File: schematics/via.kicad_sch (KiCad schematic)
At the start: 8 parts, among them SW1 SW_DIP_x08, SW2 SW_Push, SW3 SW_Push, SW5 SW_Push, SW6 SW_Push, U27 W65C22SxP, U28 74HC14

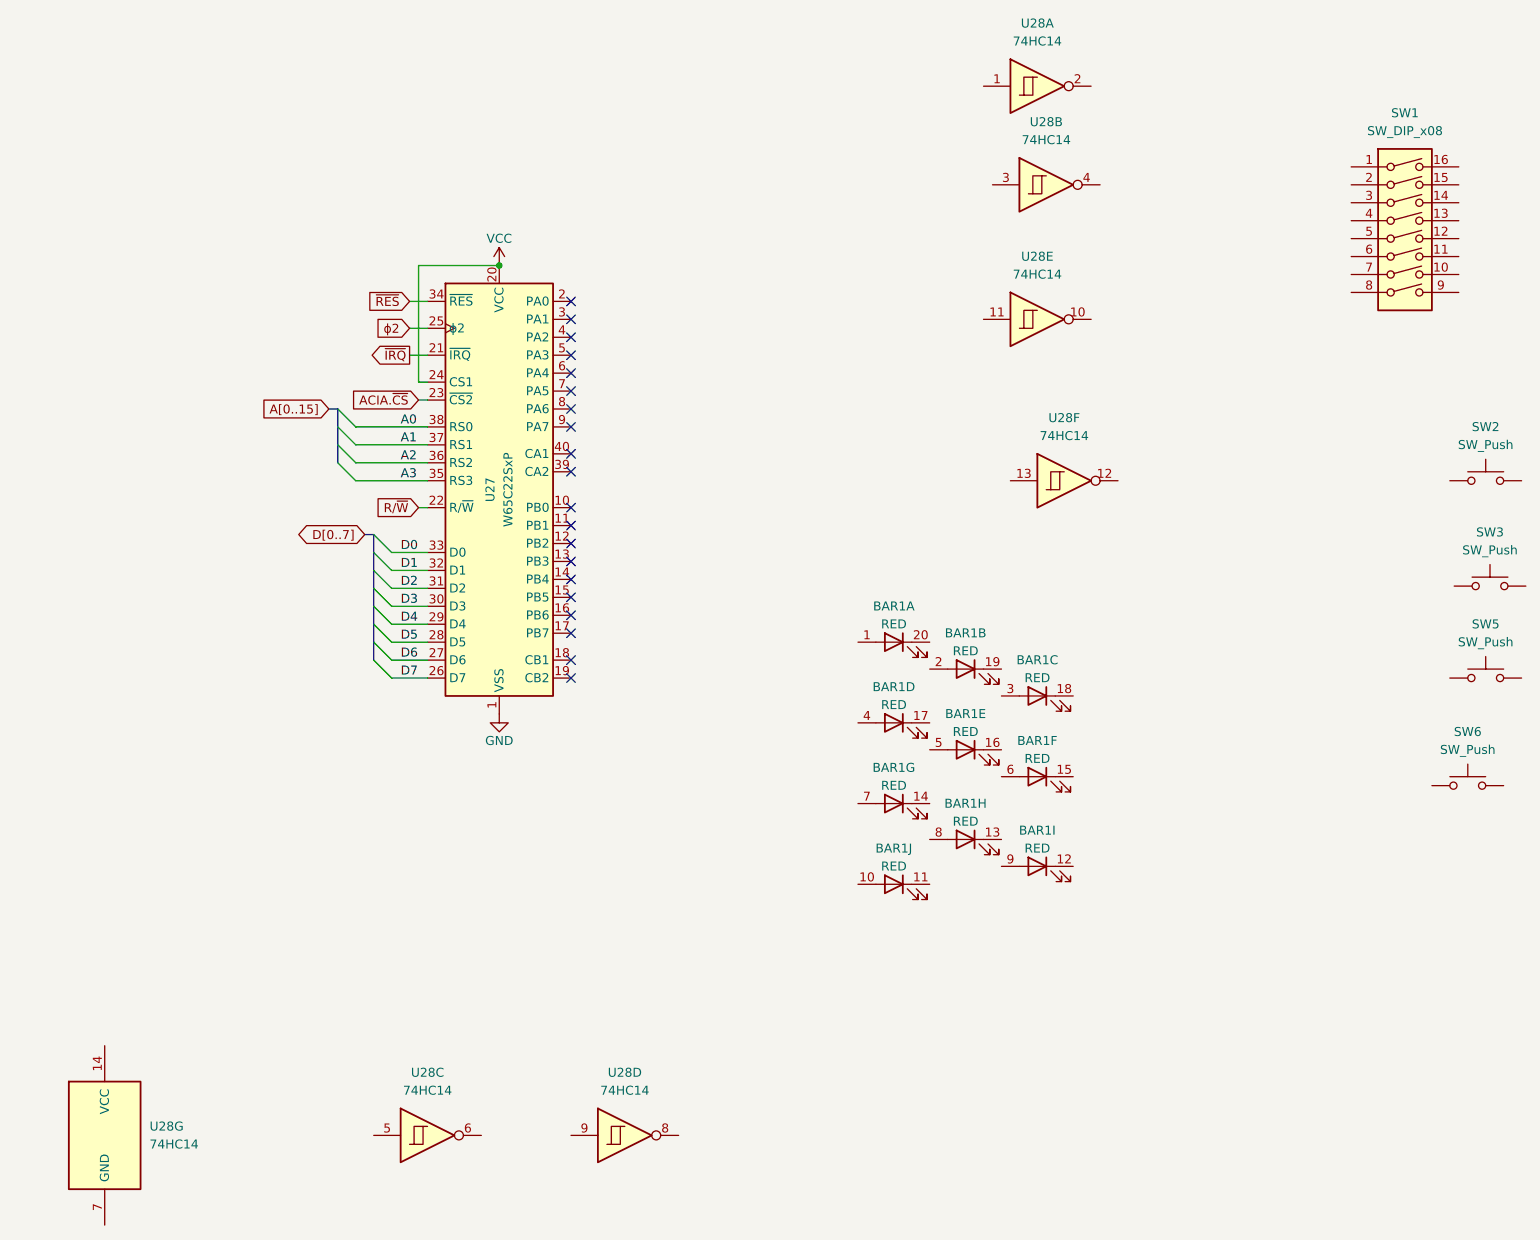
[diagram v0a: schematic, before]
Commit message: fixes to bootloader; finished via schematic
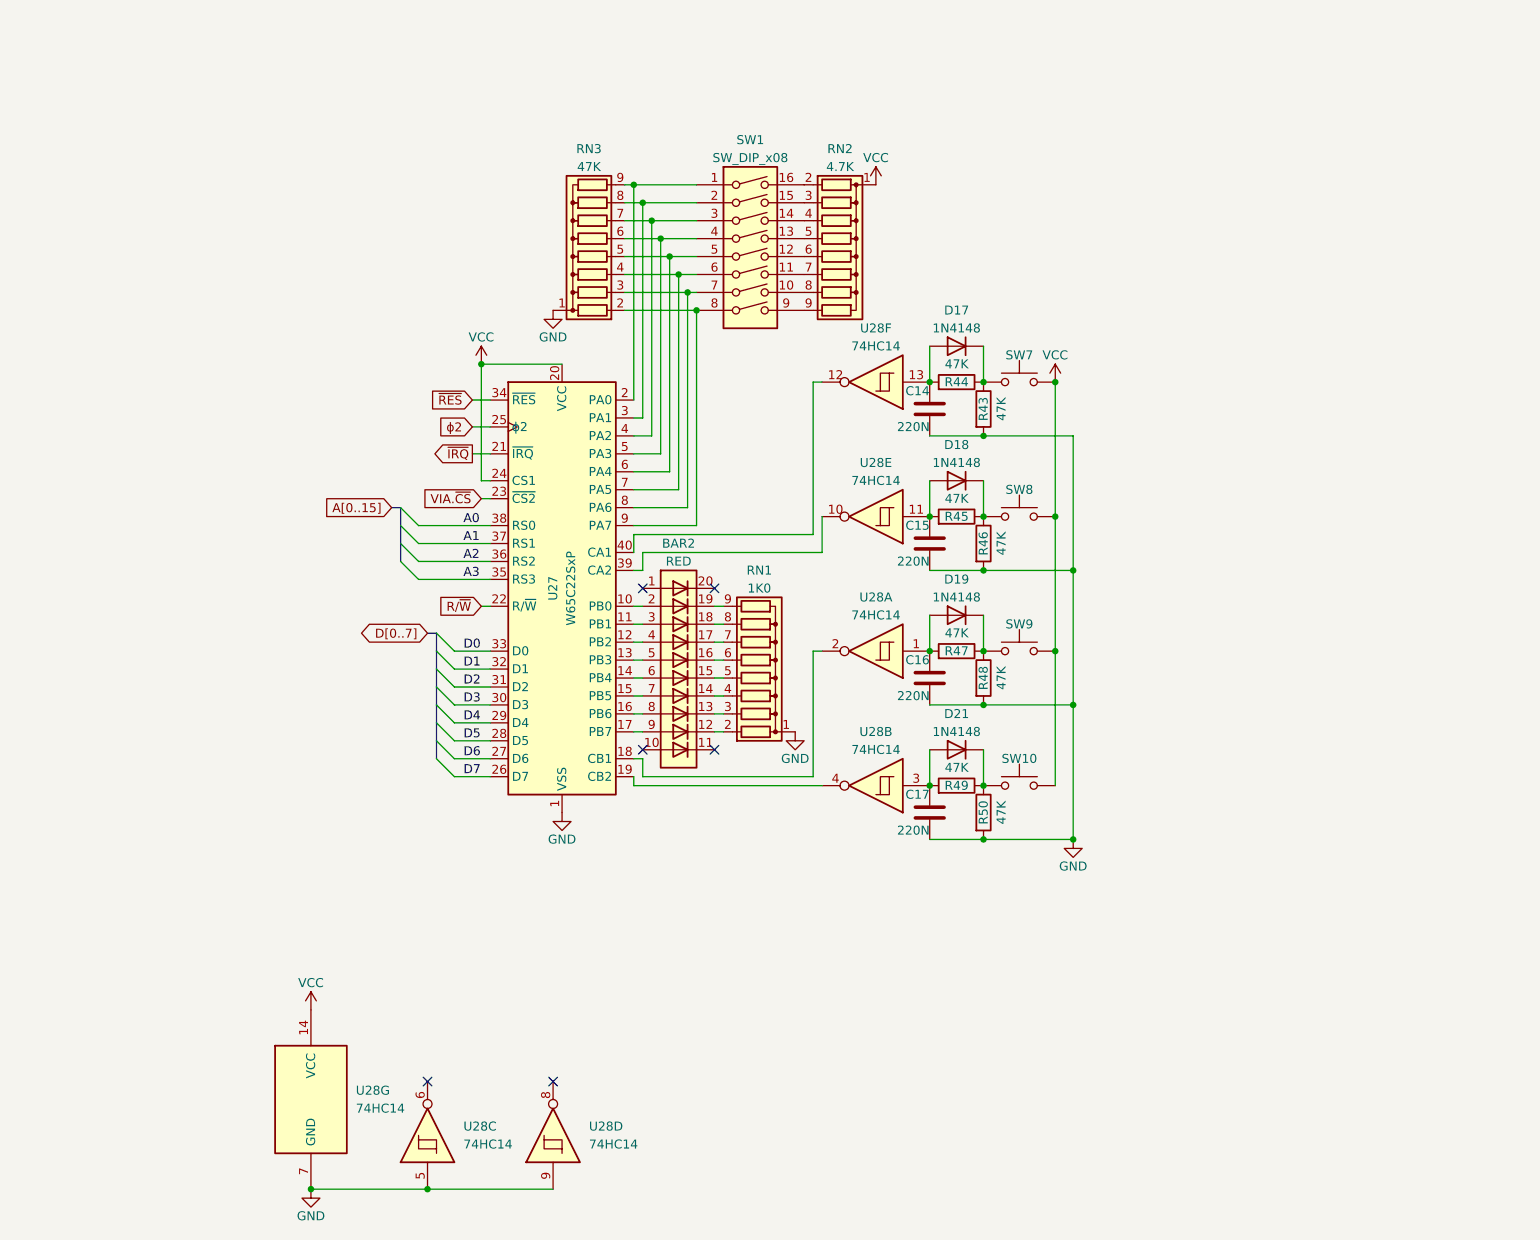
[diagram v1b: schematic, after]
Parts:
- removed BAR1: RED, Display:HDSP-4830, symbol LED:HDSP-4830
- removed SW2, SW3, SW5, SW6: SW_Push, symbol Switch:SW_Push
- added BAR2: RED, Display:HDSP-4830, symbol LED:HDSP-4830_2
- added C14, C15, C16, C17: 220N, symbol Device:C
- added D17, D18, D19, D21: 1N4148, Diode_THT:D_DO-35_SOD27_P7.62mm_Horizontal, symbol Diode:1N4148
- added R43, R44, R45, R46, R47, R48, R49, R50: 47K, symbol Device:R
- added RN1: 1K0, Resistor_THT:R_Array_SIP9, symbol Device:R_Network08
- added RN2: 4.7K, Resistor_THT:R_Array_SIP9, symbol Device:R_Network08
- added RN3: 47K, Resistor_THT:R_Array_SIP9, symbol Device:R_Network08
- added SW10, SW7, SW8, SW9: (no value), symbol Switch:SW_Push
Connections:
- net GND: now also U28.5, U28.7 (GND), U28.9, C14.1, C15.1, C16.1, C17.1, R43.2, R46.2, R48.2, R50.2, RN1.1 (common), RN3.1 (common)
- net VCC: now also U28.14 (VCC), RN2.1 (common), SW10.1, SW7.1, SW8.1, SW9.1
- net at U27.10 (PB0): now also BAR2.2 (A)
- net at U27.11 (PB1): now also BAR2.3 (A)
- net at U27.12 (PB2): now also BAR2.4 (A)
- net at U27.13 (PB3): now also BAR2.5 (A)
- net at U27.14 (PB4): now also BAR2.6 (A)
- net at U27.15 (PB5): now also BAR2.7 (A)
- net at U27.16 (PB6): now also BAR2.8 (A)
- net at U27.17 (PB7): now also BAR2.9 (A)
- net at U27.18 (CB1): now also U28.2
- net at U27.19 (CB2): now also U28.4
- net at U27.2 (PA0): now also SW1.1, RN3.9 (R8)
- net at U27.3 (PA1): now also SW1.2, RN3.8 (R7)
- net at U27.39 (CA2): now also U28.10
- net at U27.4 (PA2): now also SW1.3, RN3.7 (R6)
- net at U27.40 (CA1): now also U28.12
- net at U27.5 (PA3): now also SW1.4, RN3.6 (R5)
- net at U27.6 (PA4): now also SW1.5, RN3.5 (R4)
- net at U27.7 (PA5): now also SW1.6, RN3.4 (R3)
- net at U27.8 (PA6): now also SW1.7, RN3.3 (R2)
- net at U27.9 (PA7): now also SW1.8, RN3.2 (R1)
- net at U28.3: now also C17.2, D21.2 (A), R49.2
- net at SW1.10: now also RN2.8 (R7)
- net at SW1.11: now also RN2.7 (R6)
- net at SW1.12: now also RN2.6 (R5)
- net at SW1.13: now also RN2.5 (R4)
- net at SW1.14: now also RN2.4 (R3)
- net at SW1.15: now also RN2.3 (R2)
- net at SW1.16: now also RN2.2 (R1)
- net at SW1.9: now also RN2.9 (R8)
- net at U28.11: now also C15.2, D18.2 (A), R45.2
- net at U28.1: now also C16.2, D19.2 (A), R47.2
- net at U28.13: now also C14.2, D17.2 (A), R44.2
- net ACIA.~{CS} renamed VIA.~{CS}
- new net: BAR2.12 (K), RN1.2 (R1)
- new net: BAR2.13 (K), RN1.3 (R2)
- new net: BAR2.14 (K), RN1.4 (R3)
- new net: BAR2.15 (K), RN1.5 (R4)
- new net: BAR2.16 (K), RN1.6 (R5)
- new net: BAR2.17 (K), RN1.7 (R6)
- new net: BAR2.18 (K), RN1.8 (R7)
- new net: BAR2.19 (K), RN1.9 (R8)
- new net: D21.1 (K), R49.1, R50.1, SW10.2
- new net: D17.1 (K), R43.1, R44.1, SW7.2
- new net: D18.1 (K), R45.1, R46.1, SW8.2
- new net: D19.1 (K), R47.1, R48.1, SW9.2
- no-connect marks 20 -> 6
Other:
- moved on the sheet: SW1, U27, U28A, U28B, U28C, U28D, U28E, U28F, U28G

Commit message: updating schematics as I wire the board
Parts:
- removed RN2: 4.7K, Resistor_THT:R_Array_SIP9, symbol Device:R_Network08
- renumbered BAR2 to BAR1, C15 to C10, C16 to C11, C17 to C12, C14 to C9, D17 to D6, D18 to D7, D19 to D8, D21 to D9, R44 to R25, R45 to R26, R47 to R27, R49 to R28, R43 to R29, R46 to R30, R48 to R31, R50 to R32, RN3 to RN1, RN1 to RN2, SW1 to SW2, SW7 to SW3, SW8 to SW4, SW9 to SW5, SW10 to SW6, U28 to U16, U27 to U17
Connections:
- net VCC: now also SW2.10, SW2.11, SW2.12, SW2.13, SW2.14, SW2.15, SW2.16, SW2.9
- net at C12.2, D9.2 (A), R28.2: now also U16.5; no longer U16.3
- net at U17.19 (CB2): now also U16.6; no longer U16.4
- net at U17.39 (CA2): now also U16.8; no longer U16.10
- net at C10.2, D7.2 (A), R26.2: now also U16.9; no longer U16.11
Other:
- moved on the sheet: RN1, SW2

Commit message: updating schematics as I wire the board
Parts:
- added D16: 1N4148, Diode_THT:D_DO-35_SOD27_P7.62mm_Horizontal, symbol Diode:1N4148
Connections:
- net GND: now also SW2.10, SW2.11, SW2.12, SW2.13, SW2.14, SW2.15, SW2.16, SW2.9; no longer RN1.1 (common)
- net VCC: now also RN1.1 (common); no longer SW2.10, SW2.11, SW2.12, SW2.13, SW2.14, SW2.15, SW2.16, SW2.9
- net ~{IRQ}: now also D16.2 (A); no longer U17.21 (~{IRQ})
- net at SW2.1, U17.2 (PA0): now also RN1.2 (R1); no longer RN1.9 (R8)
- net at SW2.2, U17.3 (PA1): now also RN1.3 (R2); no longer RN1.8 (R7)
- net at SW2.3, U17.4 (PA2): now also RN1.4 (R3); no longer RN1.7 (R6)
- net at SW2.4, U17.5 (PA3): now also RN1.5 (R4); no longer RN1.6 (R5)
- net at SW2.5, U17.6 (PA4): now also RN1.6 (R5); no longer RN1.5 (R4)
- net at SW2.6, U17.7 (PA5): now also RN1.7 (R6); no longer RN1.4 (R3)
- net at SW2.7, U17.8 (PA6): now also RN1.8 (R7); no longer RN1.3 (R2)
- net at SW2.8, U17.9 (PA7): now also RN1.9 (R8); no longer RN1.2 (R1)
- new net: D16.1 (K), U17.21 (~{IRQ})
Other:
- moved on the sheet: RN1, SW2

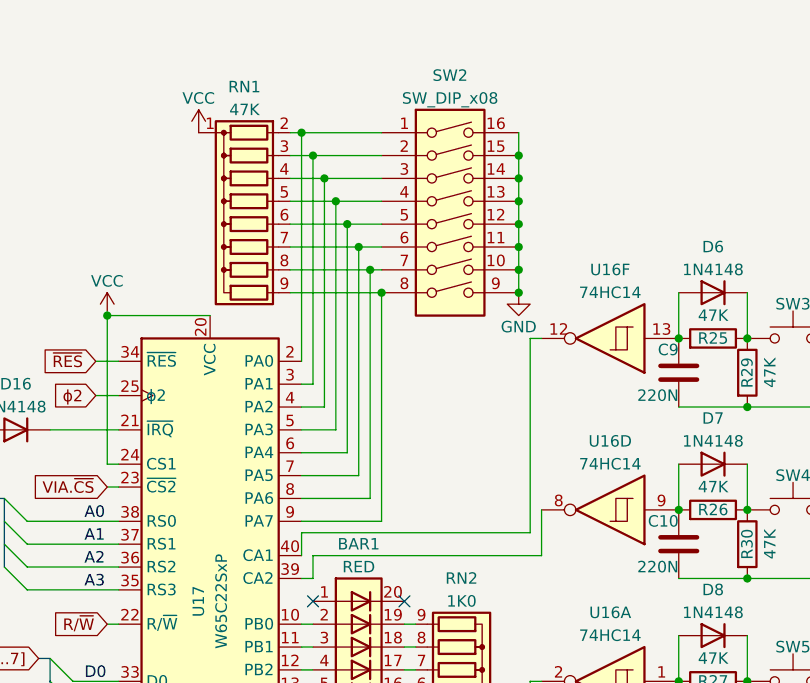
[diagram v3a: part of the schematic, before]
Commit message: pullup/pulldown on dip switch
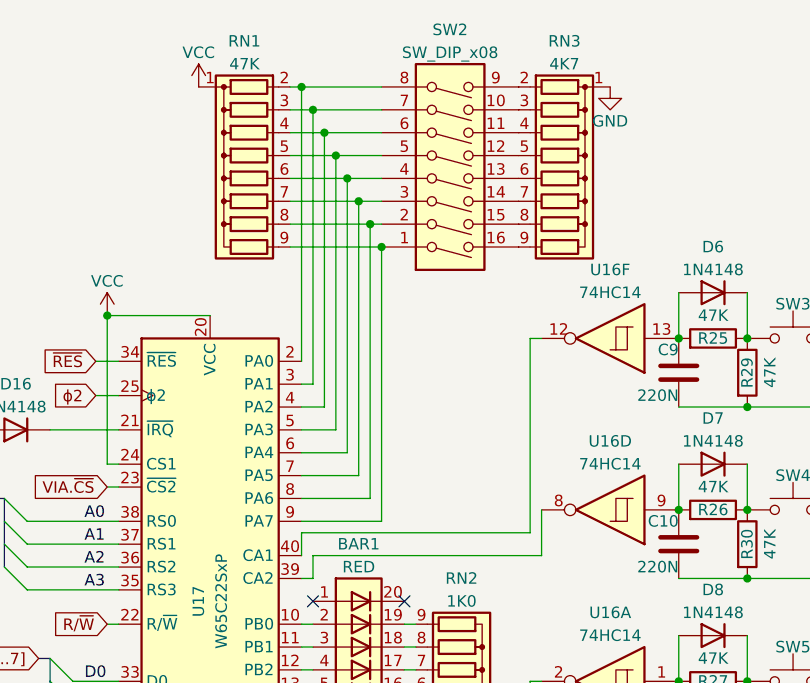
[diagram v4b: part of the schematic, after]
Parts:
- added RN3: 4K7, Resistor_THT:R_Array_SIP9, symbol Device:R_Network08
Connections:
- net GND: now also RN3.1 (common); no longer SW2.10, SW2.11, SW2.12, SW2.13, SW2.14, SW2.15, SW2.16, SW2.9
- net at RN1.2 (R1), U17.2 (PA0): now also SW2.8; no longer SW2.1
- net at RN1.3 (R2), U17.3 (PA1): now also SW2.7; no longer SW2.2
- net at RN1.4 (R3), U17.4 (PA2): now also SW2.6; no longer SW2.3
- net at RN1.5 (R4), U17.5 (PA3): now also SW2.5; no longer SW2.4
- net at RN1.6 (R5), U17.6 (PA4): now also SW2.4; no longer SW2.5
- net at RN1.7 (R6), U17.7 (PA5): now also SW2.3; no longer SW2.6
- net at RN1.8 (R7), U17.8 (PA6): now also SW2.2; no longer SW2.7
- net at RN1.9 (R8), U17.9 (PA7): now also SW2.1; no longer SW2.8
- new net: RN3.3 (R2), SW2.10
- new net: RN3.4 (R3), SW2.11
- new net: RN3.5 (R4), SW2.12
- new net: RN3.6 (R5), SW2.13
- new net: RN3.7 (R6), SW2.14
- new net: RN3.8 (R7), SW2.15
- new net: RN3.9 (R8), SW2.16
- new net: RN3.2 (R1), SW2.9
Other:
- moved on the sheet: RN1, SW2
